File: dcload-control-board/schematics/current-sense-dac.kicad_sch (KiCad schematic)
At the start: 23 parts, among them U400 NCS20231, U401 AD7091R, U402 LTC2641-16, U403 NCS20231, U404 LM4040A-5.0

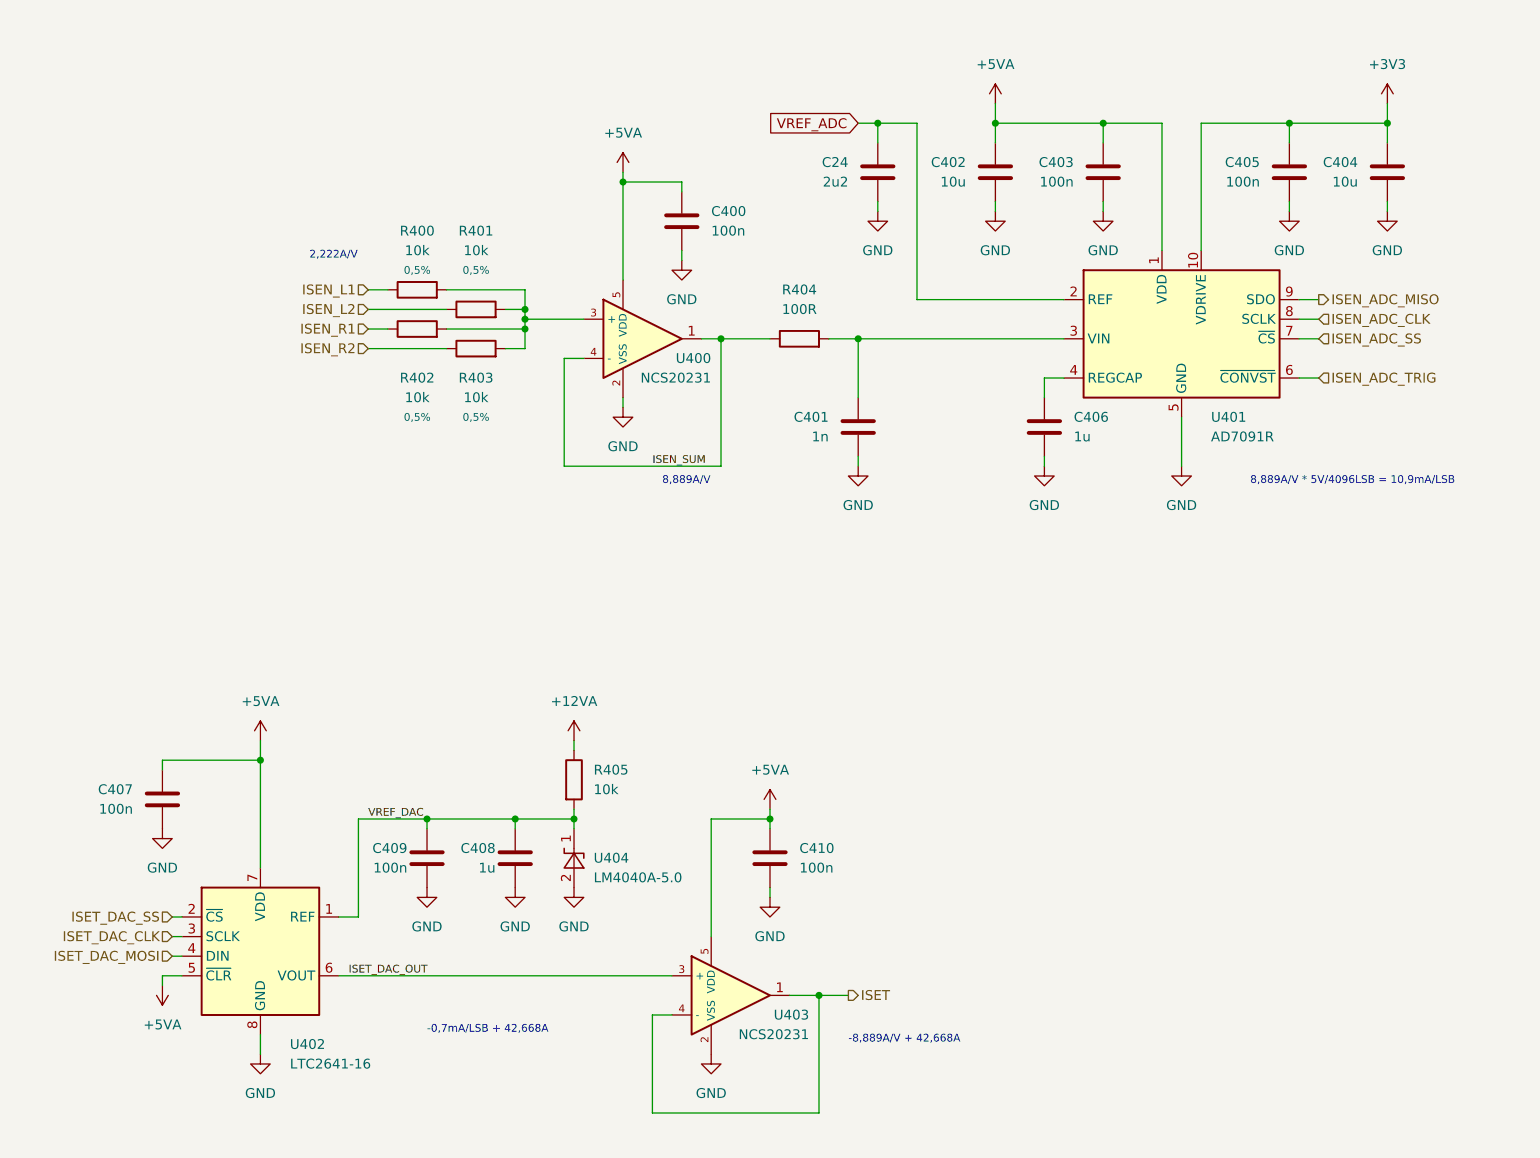
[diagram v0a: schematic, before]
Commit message: add: interface panel board
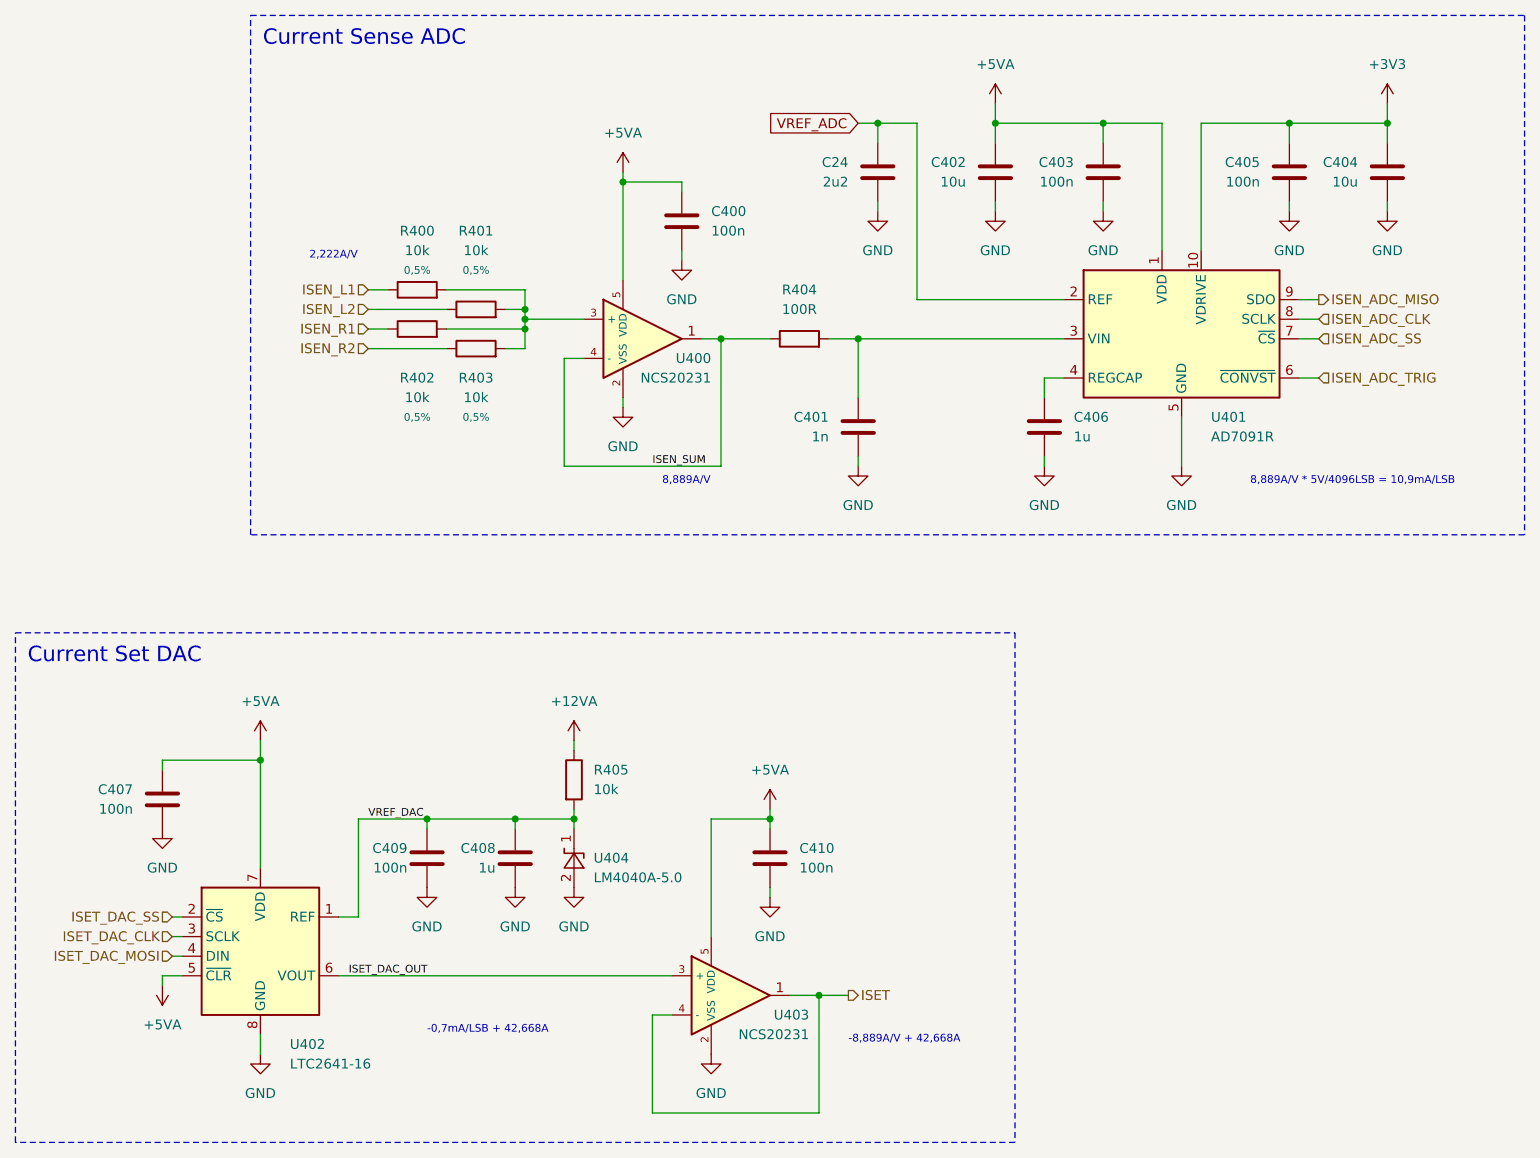
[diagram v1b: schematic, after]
